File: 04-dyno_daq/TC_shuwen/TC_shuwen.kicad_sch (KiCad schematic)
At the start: 9 parts, among them J1 Conn_01x04, J2 Conn_01x02, U1 INA333xxDGK

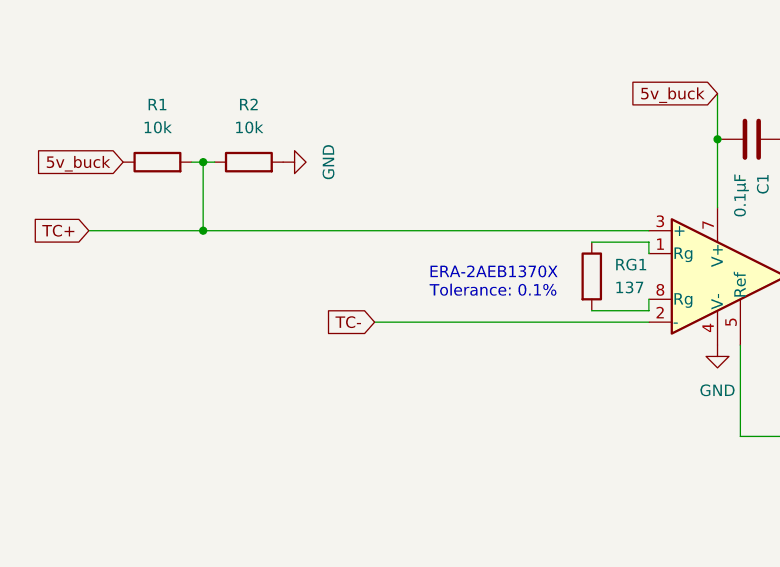
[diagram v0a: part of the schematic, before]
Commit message: Updated grounding for temp pcbs
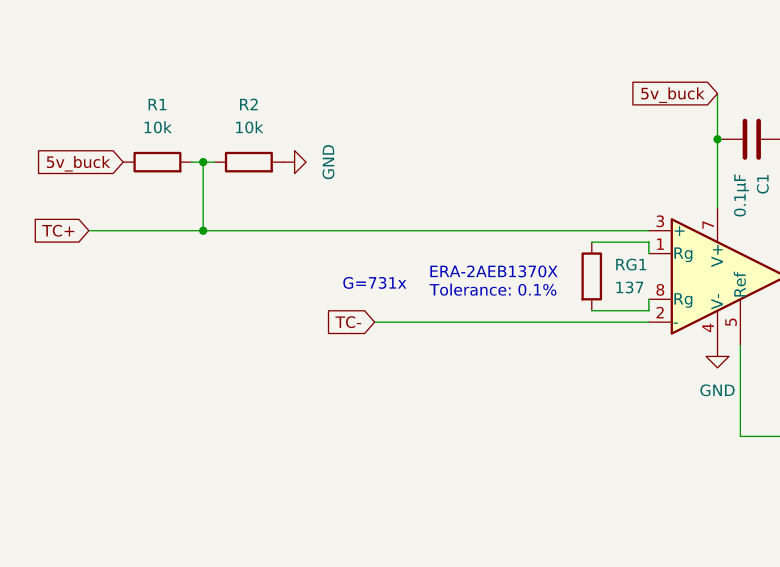
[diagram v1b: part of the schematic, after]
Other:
- note added: "G=731x"
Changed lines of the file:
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@@
+		)
+	)
+	(text "G=731x"
+		(exclude_from_sim no)
+		(at 87.63 79.756 0)
+		(effects
+			(font
+				(size 1.27 1.27)
+			)
 		)
 	)

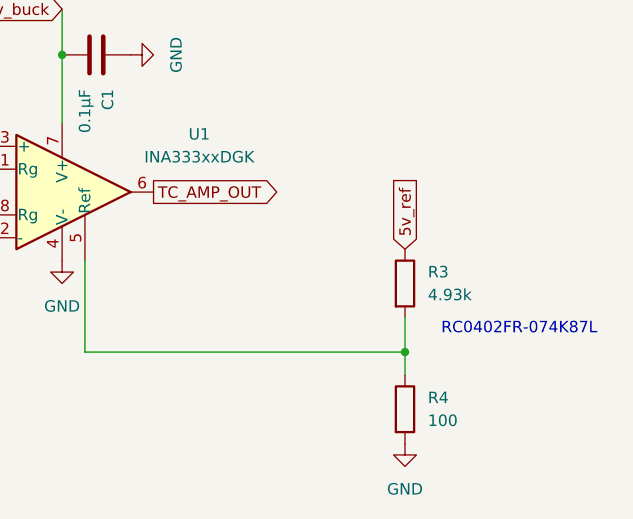
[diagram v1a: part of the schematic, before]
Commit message: Added silkscreen descriptor text + kent's name to TC shuwen
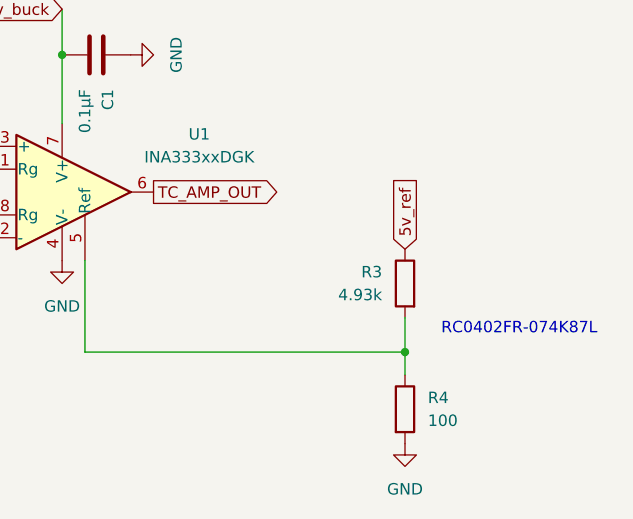
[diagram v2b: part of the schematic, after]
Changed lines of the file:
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@@
 		(lib_id "Device:R")
 		(at 163.83 88.9 0)
+		(mirror y)
 		(unit 1)
 		(exclude_from_sim no)
@@
 		(on_board yes)
 		(dnp no)
-		(fields_autoplaced yes)
 		(property "Reference" "R3"
-			(at 166.37 87.6299 0)
+			(at 161.29 87.6299 0)
 			(effects
 				(font
@@
 		)
 		(property "Value" "4.93k"
-			(at 166.37 90.1699 0)
+			(at 161.29 90.1699 0)
 			(effects
 				(font
@@
 		)
 		(property "Footprint" "Resistor_SMD:R_0402_1005Metric"
-			(at 162.052 88.9 90)
+			(at 165.608 88.9 90)
 			(effects
 				(font
